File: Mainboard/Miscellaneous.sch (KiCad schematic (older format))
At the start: 8 parts

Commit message: Modify library references
As described in the README of the newly added libraries submodule.
Schematic and PCB are synced.

Hardware folder is renamed to mainboard
Any other PCBs can be put in their own subfolder in the gitrepo

Commit also swaps source/drain of Q1 because it appeared wrong for some
reason after updating all symbol/footprints.
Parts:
- LOGO1: footprint ZOUDIOfootprints:ZOUDIO25mm -> ZOUDIO-footprints:ZOUDIO25mm
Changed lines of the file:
@@
 F 0 "LOGO1" H 6150 4425 50  0001 C CNN
 F 1 "ZOUDIO" H 6150 3900 50  0000 C CNN
-F 2 "ZOUDIOfootprints:ZOUDIO25mm" H 6150 4150 50  0001 C CNN
+F 2 "ZOUDIO-footprints:ZOUDIO25mm" H 6150 4150 50  0001 C CNN
 F 3 "~" H 6150 4150 50  0001 C CNN
 	1    6150 4150

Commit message: Before power tree change
Backup before switching from two to one LDO
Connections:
- net labels removed: +3V3, +5V, 5V_usb, VDD
- wire segments 4 -> 0
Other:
- note removed: "ERC"
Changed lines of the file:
@@
 Sheet 3 9
 Title "4x38W amp with DSP and BT"
-Date "2021-06-08"
-Rev "0.1"
+Date "2021-11-08"
+Rev "0.2"
 Comp "ZOUDIO"
 Comment1 ""
@@
 	1    0    0    -1
 $EndComp
-$Comp
-L power:+3V3 #PWR?
-U 1 1 610586CC
-P 7300 3950
-AR Path="/610586CC" Ref="#PWR?"  Part="1"
-AR Path="/5FCC1D27/610586CC" Ref="#PWR?"  Part="1"
-AR Path="/5FBDE62F/610586CC" Ref="#PWR?"  Part="1"
-AR Path="/5FD81784/610586CC" Ref="#PWR?"  Part="1"
-AR Path="/5FCDB1AE/610586CC" Ref="#PWR?"  Part="1"
-AR Path="/5FF9E05B/610586CC" Ref="#PWR?"  Part="1"
-AR Path="/60A7E145/610586CC" Ref="#PWR?"  Part="1"
-AR Path="/60AA037E/610586CC" Ref="#PWR0162"  Part="1"
-F 0 "#PWR0162" H 7300 3800 50  0001 C CNN
-F 1 "+3V3" V 7300 4200 50  0000 C CNN
-F 2 "" H 7300 3950 50  0001 C CNN
-F 3 "" H 7300 3950 50  0001 C CNN
-	1    7300 3950
-	0    -1   -1   0
-$EndComp
-Wire Wire Line
-	7350 3950 7300 3950
-$Comp
-L power:VDD #PWR?
-U 1 1 6105F88B
-P 7300 4400
-AR Path="/60B7AC16/6105F88B" Ref="#PWR?"  Part="1"
-AR Path="/60AA037E/6105F88B" Ref="#PWR0173"  Part="1"
-F 0 "#PWR0173" H 7300 4250 50  0001 C CNN
-F 1 "VDD" V 7300 4600 50  0000 C CNN
-F 2 "" H 7300 4400 50  0001 C CNN
-F 3 "" H 7300 4400 50  0001 C CNN
-	1    7300 4400
-	0    -1   -1   0
-$EndComp
-Wire Wire Line
-	7350 4400 7300 4400
-Text GLabel 7300 4250 0    50   Input ~ 0
-5V_usb
-Wire Wire Line
-	7350 4250 7300 4250
-Wire Wire Line
-	7300 4100 7350 4100
-$Comp
-L power:+5V #PWR?
-U 1 1 6105F891
-P 7300 4100
-AR Path="/60A7E145/6105F891" Ref="#PWR?"  Part="1"
-AR Path="/60E45FC0/6105F891" Ref="#PWR?"  Part="1"
-AR Path="/60B7AC16/6105F891" Ref="#PWR?"  Part="1"
-AR Path="/60AA037E/6105F891" Ref="#PWR0184"  Part="1"
-F 0 "#PWR0184" H 7300 3950 50  0001 C CNN
-F 1 "+5V" V 7300 4300 50  0000 C CNN
-F 2 "" H 7300 4100 50  0001 C CNN
-F 3 "" H 7300 4100 50  0001 C CNN
-	1    7300 4100
-	0    -1   -1   0
-$EndComp
-Wire Notes Line
-	6900 3850 7950 3850
-Wire Notes Line
-	7950 3850 7950 4500
-Wire Notes Line
-	7950 4500 6900 4500
-Wire Notes Line
-	6900 4500 6900 3850
-Text Notes 6900 3850 0    50   ~ 0
-ERC
 Wire Notes Line
 	3700 3850 4550 3850

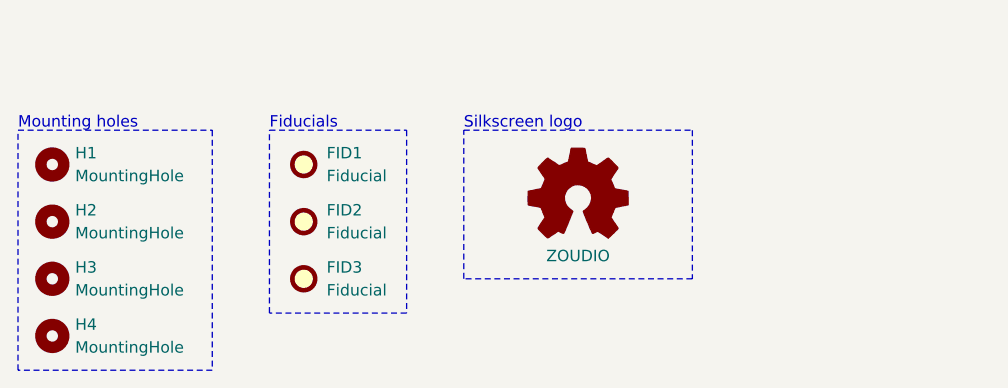
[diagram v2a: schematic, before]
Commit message: Before testing CH340B and VCHG
Cleaned up amp lay-out a bit in the meanwhile
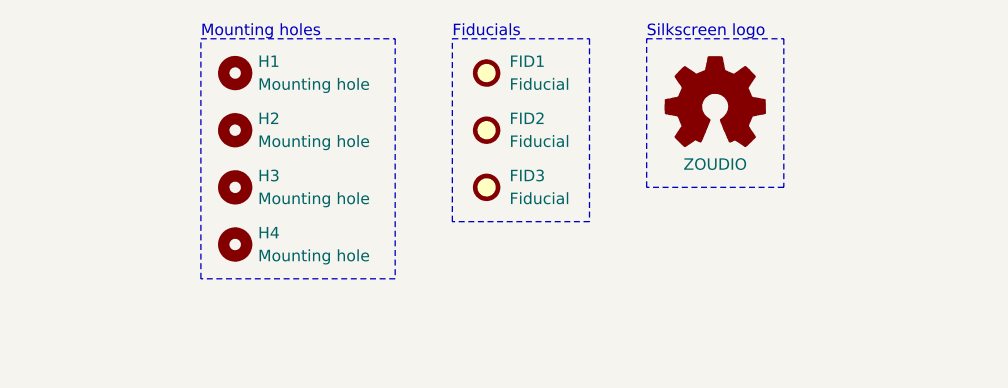
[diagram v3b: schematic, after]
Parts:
- H1, H2, H3, H4: value MountingHole -> Mounting hole
- LOGO1: Config (none) -> dnp
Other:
- moved on the sheet: FID1, FID2, FID3, H1, H2, H3, H4
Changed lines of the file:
@@
 $Descr A4 11693 8268
 encoding utf-8
-Sheet 3 9
+Sheet 2 11
 Title "4x38W amp with DSP and BT"
-Date "2021-11-08"
+Date "2021-11-19"
 Rev "0.2"
 Comp "ZOUDIO"
@@
 L Mechanical:Fiducial FID1
 U 1 1 60AA180D
-P 4950 4000
-F 0 "FID1" H 5050 4050 50  0000 L CNN
-F 1 "Fiducial" H 5050 3950 50  0000 L CNN
-F 2 "Fiducial:Fiducial_0.75mm_Dia_1.5mm_Outer" H 4950 4000 50  0001 C CNN
-F 3 "~" H 4950 4000 50  0001 C CNN
-	1    4950 4000
+P 5750 3600
+F 0 "FID1" H 5850 3650 50  0000 L CNN
+F 1 "Fiducial" H 5850 3550 50  0000 L CNN
+F 2 "Fiducial:Fiducial_0.75mm_Dia_1.5mm_Outer" H 5750 3600 50  0001 C CNN
+F 3 "~" H 5750 3600 50  0001 C CNN
+	1    5750 3600
 	1    0    0    -1
 $EndComp
@@
 L Mechanical:MountingHole H1
 U 1 1 60CB6D75
-P 3850 4000
-F 0 "H1" H 3950 4050 50  0000 L CNN
-F 1 "MountingHole" H 3950 3950 50  0000 L CNN
-F 2 "MountingHole:MountingHole_3.2mm_M3_Pad_Via" H 3850 4000 50  0001 C CNN
-F 3 "~" H 3850 4000 50  0001 C CNN
-	1    3850 4000
+P 4650 3600
+F 0 "H1" H 4750 3650 50  0000 L CNN
+F 1 "Mounting hole" H 4750 3550 50  0000 L CNN
+F 2 "MountingHole:MountingHole_3.2mm_M3_Pad_Via" H 4650 3600 50  0001 C CNN
+F 3 "~" H 4650 3600 50  0001 C CNN
+	1    4650 3600
 	1    0    0    -1
 $EndComp
@@
 L Mechanical:MountingHole H2
 U 1 1 60CB7225
-P 3850 4250
-F 0 "H2" H 3950 4300 50  0000 L CNN
-F 1 "MountingHole" H 3950 4200 50  0000 L CNN
-F 2 "MountingHole:MountingHole_3.2mm_M3_Pad_Via" H 3850 4250 50  0001 C CNN
-F 3 "~" H 3850 4250 50  0001 C CNN
-	1    3850 4250
+P 4650 3850
+F 0 "H2" H 4750 3900 50  0000 L CNN
+F 1 "Mounting hole" H 4750 3800 50  0000 L CNN
+F 2 "MountingHole:MountingHole_3.2mm_M3_Pad_Via" H 4650 3850 50  0001 C CNN
+F 3 "~" H 4650 3850 50  0001 C CNN
+	1    4650 3850
 	1    0    0    -1
 $EndComp
@@
 L Mechanical:MountingHole H3
 U 1 1 60CB73BB
-P 3850 4500
-F 0 "H3" H 3950 4550 50  0000 L CNN
-F 1 "MountingHole" H 3950 4450 50  0000 L CNN
-F 2 "MountingHole:MountingHole_3.2mm_M3_Pad_Via" H 3850 4500 50  0001 C CNN
-F 3 "~" H 3850 4500 50  0001 C CNN
-	1    3850 4500
+P 4650 4100
+F 0 "H3" H 4750 4150 50  0000 L CNN
+F 1 "Mounting hole" H 4750 4050 50  0000 L CNN
+F 2 "MountingHole:MountingHole_3.2mm_M3_Pad_Via" H 4650 4100 50  0001 C CNN
+F 3 "~" H 4650 4100 50  0001 C CNN
+	1    4650 4100
 	1    0    0    -1
 $EndComp
@@
 L Mechanical:MountingHole H4
 U 1 1 60CB7656
-P 3850 4750
-F 0 "H4" H 3950 4800 50  0000 L CNN
-F 1 "MountingHole" H 3950 4700 50  0000 L CNN
-F 2 "MountingHole:MountingHole_3.2mm_M3_Pad_Via" H 3850 4750 50  0001 C CNN
-F 3 "~" H 3850 4750 50  0001 C CNN
-	1    3850 4750
+P 4650 4350
+F 0 "H4" H 4750 4400 50  0000 L CNN
+F 1 "Mounting hole" H 4750 4300 50  0000 L CNN
+F 2 "MountingHole:MountingHole_3.2mm_M3_Pad_Via" H 4650 4350 50  0001 C CNN
+F 3 "~" H 4650 4350 50  0001 C CNN
+	1    4650 4350
 	1    0    0    -1
 $EndComp
@@
 L Graphic:Logo_Open_Hardware_Small LOGO1
 U 1 1 60CB7B57
-P 6150 4150
-F 0 "LOGO1" H 6150 4425 50  0001 C CNN
-F 1 "ZOUDIO" H 6150 3900 50  0000 C CNN
-F 2 "ZOUDIO-footprints:ZOUDIO25mm" H 6150 4150 50  0001 C CNN
-F 3 "~" H 6150 4150 50  0001 C CNN
-	1    6150 4150
+P 6750 3750
+F 0 "LOGO1" H 6750 4025 50  0001 C CNN
+F 1 "ZOUDIO" H 6750 3500 50  0000 C CNN
+F 2 "ZOUDIO-footprints:ZOUDIO25mm" H 6750 3750 50  0001 C CNN
+F 3 "~" H 6750 3750 50  0001 C CNN
+F 4 "dnp" H 6750 3750 50  0001 C CNN "Config"
+	1    6750 3750
 	1    0    0    -1
 $EndComp
@@
 L Mechanical:Fiducial FID2
 U 1 1 60CD5903
-P 4950 4250
-F 0 "FID2" H 5050 4300 50  0000 L CNN
-F 1 "Fiducial" H 5050 4200 50  0000 L CNN
-F 2 "Fiducial:Fiducial_0.75mm_Dia_1.5mm_Outer" H 4950 4250 50  0001 C CNN
-F 3 "~" H 4950 4250 50  0001 C CNN
-	1    4950 4250
+P 5750 3850
+F 0 "FID2" H 5850 3900 50  0000 L CNN
+F 1 "Fiducial" H 5850 3800 50  0000 L CNN
+F 2 "Fiducial:Fiducial_0.75mm_Dia_1.5mm_Outer" H 5750 3850 50  0001 C CNN
+F 3 "~" H 5750 3850 50  0001 C CNN
+	1    5750 3850
 	1    0    0    -1
 $EndComp
@@
 L Mechanical:Fiducial FID3
 U 1 1 60CD5AD1
-P 4950 4500
-F 0 "FID3" H 5050 4550 50  0000 L CNN
-F 1 "Fiducial" H 5050 4450 50  0000 L CNN
-F 2 "Fiducial:Fiducial_0.75mm_Dia_1.5mm_Outer" H 4950 4500 50  0001 C CNN
-F 3 "~" H 4950 4500 50  0001 C CNN
-	1    4950 4500
+P 5750 4100
+F 0 "FID3" H 5850 4150 50  0000 L CNN
+F 1 "Fiducial" H 5850 4050 50  0000 L CNN
+F 2 "Fiducial:Fiducial_0.75mm_Dia_1.5mm_Outer" H 5750 4100 50  0001 C CNN
+F 3 "~" H 5750 4100 50  0001 C CNN
+	1    5750 4100
 	1    0    0    -1
 $EndComp
 Wire Notes Line
-	3700 3850 4550 3850
+	4500 3450 5350 3450
 Wire Notes Line
-	4550 3850 4550 4900
+	5350 3450 5350 4500
 Wire Notes Line
-	4550 4900 3700 4900
+	5350 4500 4500 4500
 Wire Notes Line
-	3700 4900 3700 3850
+	4500 4500 4500 3450
 Wire Notes Line
-	4800 3850 5400 3850
+	5600 3450 6200 3450
 Wire Notes Line
-	5400 3850 5400 4650
+	6200 3450 6200 4250
 Wire Notes Line
-	5400 4650 4800 4650
+	6200 4250 5600 4250
 Wire Notes Line
-	4800 4650 4800 3850
+	5600 4250 5600 3450
 Wire Notes Line
-	5650 3850 6650 3850
+	6450 3450 7050 3450
 Wire Notes Line
-	6650 3850 6650 4500
+	7050 3450 7050 4100
 Wire Notes Line
-	6650 4500 5650 4500
+	7050 4100 6450 4100
 Wire Notes Line
-	5650 4500 5650 3850
-Text Notes 5650 3850 0    50   ~ 0
+	6450 4100 6450 3450
+Text Notes 6450 3450 0    50   ~ 0
 Silkscreen logo
-Text Notes 4800 3850 0    50   ~ 0
+Text Notes 5600 3450 0    50   ~ 0
 Fiducials
-Text Notes 3700 3850 0    50   ~ 0
+Text Notes 4500 3450 0    50   ~ 0
 Mounting holes
 $EndSCHEMATC

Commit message: Mainboard: Version 1.0
Still need to clean up 3D models and BoM list,
but gerberexport-ready and ready to order.
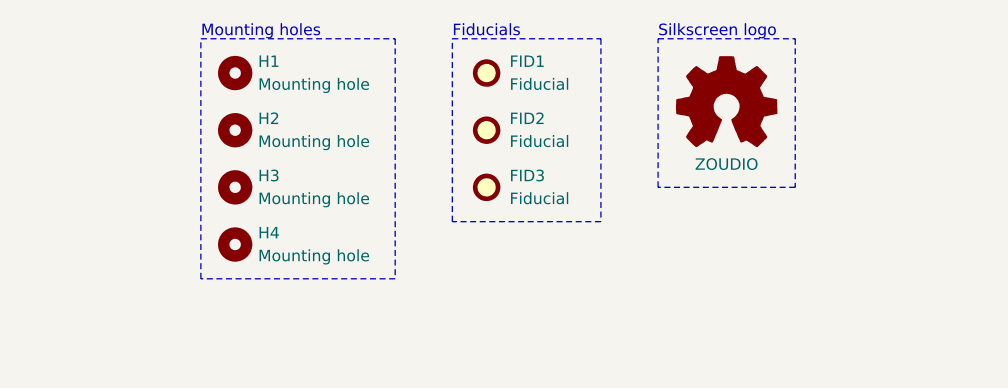
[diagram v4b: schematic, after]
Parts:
- LOGO1: footprint ZOUDIO-footprints:ZOUDIO25mm -> ZOUDIO-footprints:ZOUDIO25mm_mask
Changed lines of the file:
@@
 Sheet 2 11
 Title "4x38W amp with DSP and BT"
-Date "2021-11-19"
-Rev "0.2"
+Date "2021-12-01"
+Rev "1.0"
 Comp "ZOUDIO"
 Comment1 ""
@@
 Comment4 ""
 $EndDescr
-$Comp
-L Mechanical:Fiducial FID1
-U 1 1 60AA180D
-P 5750 3600
-F 0 "FID1" H 5850 3650 50  0000 L CNN
-F 1 "Fiducial" H 5850 3550 50  0000 L CNN
-F 2 "Fiducial:Fiducial_0.75mm_Dia_1.5mm_Outer" H 5750 3600 50  0001 C CNN
-F 3 "~" H 5750 3600 50  0001 C CNN
-	1    5750 3600
-	1    0    0    -1
-$EndComp
 $Comp
 L Mechanical:MountingHole H1
@@
 L Graphic:Logo_Open_Hardware_Small LOGO1
 U 1 1 60CB7B57
-P 6750 3750
-F 0 "LOGO1" H 6750 4025 50  0001 C CNN
-F 1 "ZOUDIO" H 6750 3500 50  0000 C CNN
-F 2 "ZOUDIO-footprints:ZOUDIO25mm" H 6750 3750 50  0001 C CNN
-F 3 "~" H 6750 3750 50  0001 C CNN
-F 4 "dnp" H 6750 3750 50  0001 C CNN "Config"
-	1    6750 3750
+P 6800 3750
+F 0 "LOGO1" H 6800 4025 50  0001 C CNN
+F 1 "ZOUDIO" H 6800 3500 50  0000 C CNN
+F 2 "ZOUDIO-footprints:ZOUDIO25mm_mask" H 6800 3750 50  0001 C CNN
+F 3 "~" H 6800 3750 50  0001 C CNN
+F 4 "dnp" H 6800 3750 50  0001 C CNN "Config"
+	1    6800 3750
+	1    0    0    -1
+$EndComp
+Wire Notes Line
+	4500 3450 5350 3450
+Wire Notes Line
+	5350 3450 5350 4500
+Wire Notes Line
+	5350 4500 4500 4500
+Wire Notes Line
+	4500 4500 4500 3450
+Wire Notes Line
+	5600 3450 6250 3450
+Wire Notes Line
+	6250 3450 6250 4250
+Wire Notes Line
+	6250 4250 5600 4250
+Wire Notes Line
+	5600 4250 5600 3450
+Wire Notes Line
+	6500 3450 7100 3450
+Wire Notes Line
+	7100 3450 7100 4100
+Wire Notes Line
+	7100 4100 6500 4100
+Wire Notes Line
+	6500 4100 6500 3450
+Text Notes 6500 3450 0    50   ~ 0
+Silkscreen logo
+Text Notes 5600 3450 0    50   ~ 0
+Fiducials
+Text Notes 4500 3450 0    50   ~ 0
+Mounting holes
+$Comp
+L Mechanical:Fiducial FID3
+U 1 1 60CD5AD1
+P 5750 4100
+F 0 "FID3" H 5850 4150 50  0000 L CNN
+F 1 "Fiducial" H 5850 4050 50  0000 L CNN
+F 2 "Fiducial:Fiducial_0.75mm_Dia_1.5mm_Outer" H 5750 4100 50  0001 C CNN
+F 3 "~" H 5750 4100 50  0001 C CNN
+	1    5750 4100
 	1    0    0    -1
 $EndComp
@@
 $EndComp
 $Comp
-L Mechanical:Fiducial FID3
-U 1 1 60CD5AD1
-P 5750 4100
-F 0 "FID3" H 5850 4150 50  0000 L CNN
-F 1 "Fiducial" H 5850 4050 50  0000 L CNN
-F 2 "Fiducial:Fiducial_0.75mm_Dia_1.5mm_Outer" H 5750 4100 50  0001 C CNN
-F 3 "~" H 5750 4100 50  0001 C CNN
-	1    5750 4100
+L Mechanical:Fiducial FID1
+U 1 1 60AA180D
+P 5750 3600
+F 0 "FID1" H 5850 3650 50  0000 L CNN
+F 1 "Fiducial" H 5850 3550 50  0000 L CNN
+F 2 "Fiducial:Fiducial_0.75mm_Dia_1.5mm_Outer" H 5750 3600 50  0001 C CNN
+F 3 "~" H 5750 3600 50  0001 C CNN
+	1    5750 3600
 	1    0    0    -1
 $EndComp
-Wire Notes Line
-	4500 3450 5350 3450
-Wire Notes Line
-	5350 3450 5350 4500
-Wire Notes Line
-	5350 4500 4500 4500
-Wire Notes Line
-	4500 4500 4500 3450
-Wire Notes Line
-	5600 3450 6200 3450
-Wire Notes Line
-	6200 3450 6200 4250
-Wire Notes Line
-	6200 4250 5600 4250
-Wire Notes Line
-	5600 4250 5600 3450
-Wire Notes Line
-	6450 3450 7050 3450
-Wire Notes Line
-	7050 3450 7050 4100
-Wire Notes Line
-	7050 4100 6450 4100
-Wire Notes Line
-	6450 4100 6450 3450
-Text Notes 6450 3450 0    50   ~ 0
-Silkscreen logo
-Text Notes 5600 3450 0    50   ~ 0
-Fiducials
-Text Notes 4500 3450 0    50   ~ 0
-Mounting holes
 $EndSCHEMATC

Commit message: Clean up schematic for BoM export
- Change 22u 0805's (amp decoupling) to 15u
- Change 680n 0805's (part of output filter) to 470n
- Change C1 (amp bulk cap) from 820u to 1000u
- Add BoM.ini for KiBom export and
- Complete fields needed for KiBom (Manufacturer and partnumber)
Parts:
- FID1, FID2, FID3, H1, H2, H3, H4: Config (none) -> dnp
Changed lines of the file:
@@
 F 2 "MountingHole:MountingHole_3.2mm_M3_Pad_Via" H 4650 3600 50  0001 C CNN
 F 3 "~" H 4650 3600 50  0001 C CNN
+F 4 "dnp" H 4650 3600 50  0001 C CNN "Config"
 	1    4650 3600
 	1    0    0    -1
@@
 F 2 "MountingHole:MountingHole_3.2mm_M3_Pad_Via" H 4650 3850 50  0001 C CNN
 F 3 "~" H 4650 3850 50  0001 C CNN
+F 4 "dnp" H 4650 3850 50  0001 C CNN "Config"
 	1    4650 3850
 	1    0    0    -1
@@
 F 2 "MountingHole:MountingHole_3.2mm_M3_Pad_Via" H 4650 4100 50  0001 C CNN
 F 3 "~" H 4650 4100 50  0001 C CNN
+F 4 "dnp" H 4650 4100 50  0001 C CNN "Config"
 	1    4650 4100
 	1    0    0    -1
@@
 F 2 "MountingHole:MountingHole_3.2mm_M3_Pad_Via" H 4650 4350 50  0001 C CNN
 F 3 "~" H 4650 4350 50  0001 C CNN
+F 4 "dnp" H 4650 4350 50  0001 C CNN "Config"
 	1    4650 4350
 	1    0    0    -1
@@
 F 2 "Fiducial:Fiducial_0.75mm_Dia_1.5mm_Outer" H 5750 4100 50  0001 C CNN
 F 3 "~" H 5750 4100 50  0001 C CNN
+F 4 "dnp" H 5750 4100 50  0001 C CNN "Config"
 	1    5750 4100
 	1    0    0    -1
@@
 F 2 "Fiducial:Fiducial_0.75mm_Dia_1.5mm_Outer" H 5750 3850 50  0001 C CNN
 F 3 "~" H 5750 3850 50  0001 C CNN
+F 4 "dnp" H 5750 3850 50  0001 C CNN "Config"
 	1    5750 3850
 	1    0    0    -1
@@
 F 2 "Fiducial:Fiducial_0.75mm_Dia_1.5mm_Outer" H 5750 3600 50  0001 C CNN
 F 3 "~" H 5750 3600 50  0001 C CNN
+F 4 "dnp" H 5750 3600 50  0001 C CNN "Config"
 	1    5750 3600
 	1    0    0    -1
